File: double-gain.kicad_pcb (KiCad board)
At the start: 2 copper layers, 32 parts, among them J1 Conn_01x01_Female, J2 pin2, J3 Conn_01x01_Female, J4 pin3, J5 pin1, J6 Conn_01x01_Female, J7 Conn_01x01_Female, J8 Conn_01x01_Female, J9 Conn_01x01_Female, U1 NE5534, U2 NE5534

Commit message: Add files via upload
updated files, corrected error
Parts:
- added C9: 22pF, Capacitor_THT:C_Disc_D5.0mm_W2.5mm_P2.50mm, F.Cu at (57.0, 80.0)
- R2: value 30K -> 4K
- R9: value 1K -> 100
- moved U2 2.50 mm to (70.0, 86.0)
- moved U1 2.00 mm to (51.0, 86.0)
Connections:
- U2 pad 2: Net-(R8-Pad2) -> Net-(R2-Pad1)
- U2 pad 3: Net-(R2-Pad1) -> Net-(R8-Pad2)
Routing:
- net Net-(R2-Pad1): track 40.7 -> 51.2 mm, vias 0 -> 1
- net Net-(C9-Pad1): track 0.00 -> 8.23 mm
- net V-: track 113.9 -> 119.7 mm
- net Net-(C9-Pad2): track 0.00 -> 5.74 mm
- net VCC: track 82.5 -> 86.4 mm, vias 0 -> 1
- net Net-(R8-Pad2): track 23.7 -> 20.7 mm
- net Net-(R2-Pad2): track 23.0 -> 25.8 mm
- net Net-(C5-Pad1): track 43.7 -> 45.7 mm
- net Earth: vias 4 -> 5
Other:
- board outline added: 37.5 x 97.5 mm
- board text added: "R2 Gain values in dB: 2K=26,3K=29,4K=32,5K=34,6K=35, 7K=37"
- board text removed: "R2 Gain values in dB:20K=26,30K=29,40K=32,50K=34,60K=35"

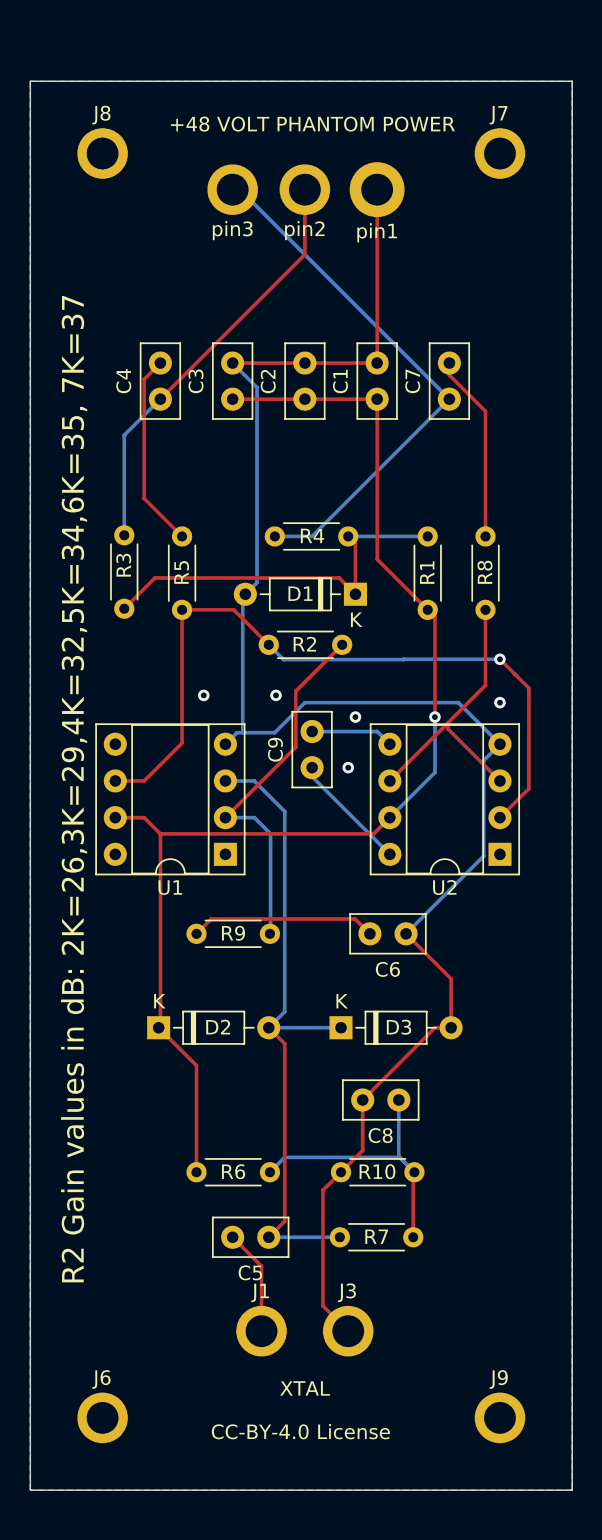
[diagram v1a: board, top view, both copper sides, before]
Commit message: Add files via upload
Converted to balanced input and output.
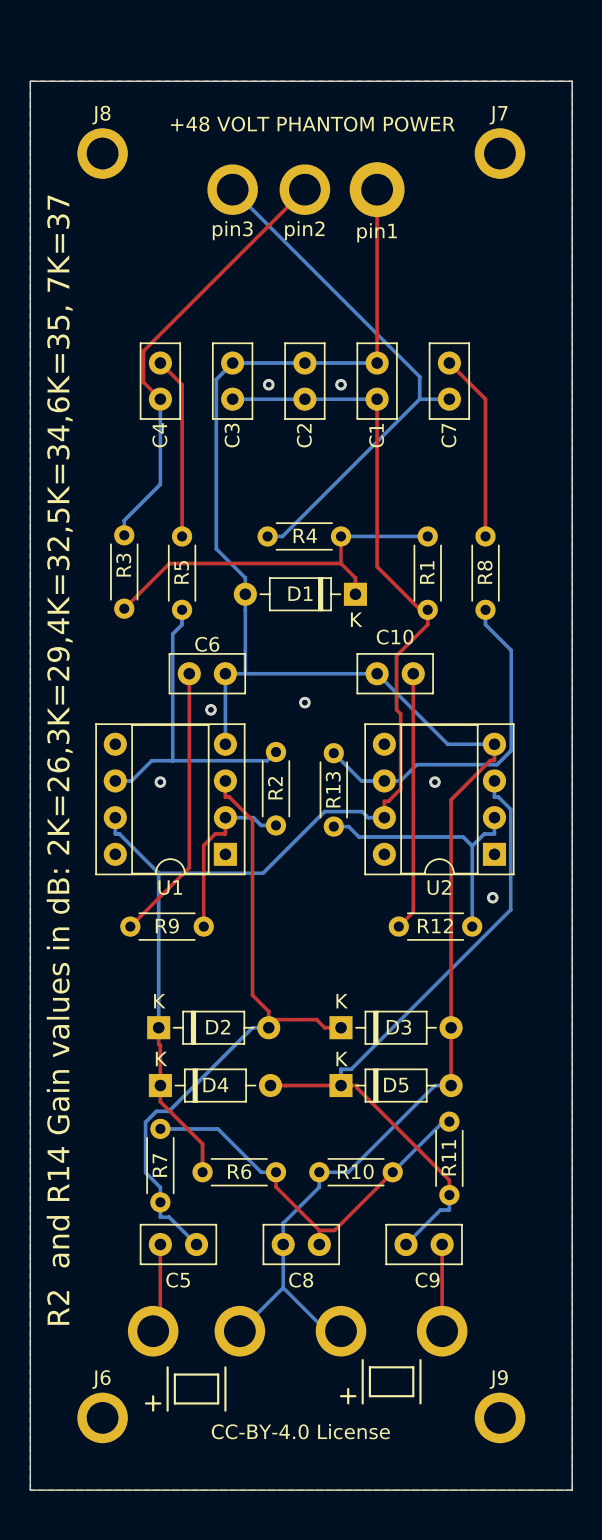
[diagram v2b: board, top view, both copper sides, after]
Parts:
- added C10: 47uF, Capacitor_THT:C_Disc_D5.0mm_W2.5mm_P2.50mm, F.Cu at (61.5, 73.5)
- added D4: 1N4148, Diode_THT:D_DO-35_SOD27_P7.62mm_Horizontal, F.Cu at (46.5, 102.0)
- added D5: 1N4148, Diode_THT:D_DO-35_SOD27_P7.62mm_Horizontal, F.Cu at (59.0, 102.0)
- added J10: Conn_01x01_Female, MountingHole:MountingHole_2.2mm_M2_ISO7380_Pad, F.Cu at (66.0, 119.0)
- added J11: Conn_01x01_Female, MountingHole:MountingHole_2.2mm_M2_ISO7380_Pad, F.Cu at (59.0, 119.0)
- added R11: 1M, Resistor_THT:R_Axial_DIN0204_L3.6mm_D1.6mm_P5.08mm_Horizontal, F.Cu at (66.5, 104.5)
- added R12: 100, Resistor_THT:R_Axial_DIN0204_L3.6mm_D1.6mm_P5.08mm_Horizontal, F.Cu at (63.0, 91.0)
- added R13: 4K, Resistor_THT:R_Axial_DIN0204_L3.6mm_D1.6mm_P5.08mm_Horizontal, F.Cu at (58.5, 79.0)
- C9: value 22pF -> 10uF
- D1: value 1N936B ( 9V ) -> 1N4746A (18V)
- moved C9 33.6 mm to (63.5, 113.0), turned to 0 degrees
- moved C6 21.9 mm to (51.0, 73.5)
- moved R7 19.0 mm to (46.5, 105.0), turned to 270 degrees
- moved C8 11.4 mm to (57.5, 113.0)
- moved J1 7.50 mm to (46.0, 119.0)
- moved J3 7.50 mm to (52.0, 119.0)
- moved R2 7.44 mm to (54.5, 78.9), turned to 270 degrees
- moved C5 5.02 mm to (49.0, 113.0)
- moved R9 4.61 mm to (44.4, 91.0)
- moved R10 1.50 mm to (62.6, 108.0)
- moved R4 0.50 mm to (59.0, 64.0)
- moved R6 0.42 mm to (49.4, 108.0)
- moved U2 0.38 mm to (69.6, 86.0)
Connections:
- C9 pad 1: Net-(C9-Pad1) -> ind
- R8 pad 2: Net-(R8-Pad2) -> Net-(R13-Pad1)
- U2 pad 2: Net-(R2-Pad1) -> Net-(R12-Pad2)
- U2 pad 3: Net-(R8-Pad2) -> ind
- U2 pad 5: Net-(C9-Pad2) -> Net-(U2-Pad5)
- U2 pad 6: Net-(R8-Pad2) -> Net-(R13-Pad1)
- U2 pad 8: Net-(C9-Pad1) -> Net-(U2-Pad8)
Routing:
- net ind: track 0.00 -> 48.2 mm
- net Net-(R2-Pad1): track 51.2 -> 22.7 mm, vias 1 -> 0
- net Net-(R13-Pad1): track 0.00 -> 24.4 mm
- net Net-(R8-Pad2): track 20.7 -> 0.00 mm
- net Net-(R12-Pad2): track 0.00 -> 18.7 mm
- net Net-(C10-Pad2): track 0.00 -> 17.9 mm
- net Net-(R2-Pad2): track 25.8 -> 12.3 mm
- net Net-(C9-Pad1): track 8.23 -> 0.00 mm
- net Net-(C8-Pad1): track 20.8 -> 27.6 mm
- net Net-(C6-Pad2): track 12.8 -> 19.2 mm
- net V-: track 119.7 -> 125.5 mm
- net Net-(C5-Pad2): track 7.33 -> 6.21 mm
- net Net-(C4-Pad1): track 29.1 -> 30.1 mm
- net VCC: track 86.4 -> 87.3 mm, vias 1 -> 0
- net Net-(C4-Pad2): track 13.6 -> 12.6 mm
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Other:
- board text added: "R2 and R14 Gain values in dB: 2K=26,3K=29,4K=32,5K=34,6K=35, 7K=37"
- board text removed: "R2 Gain values in dB: 2K=26,3K=29,4K=32,5K=34,6K=35, 7K=37"
- board text removed: "XTAL"

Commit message: Add files via upload
corrected fault, R14 is R13
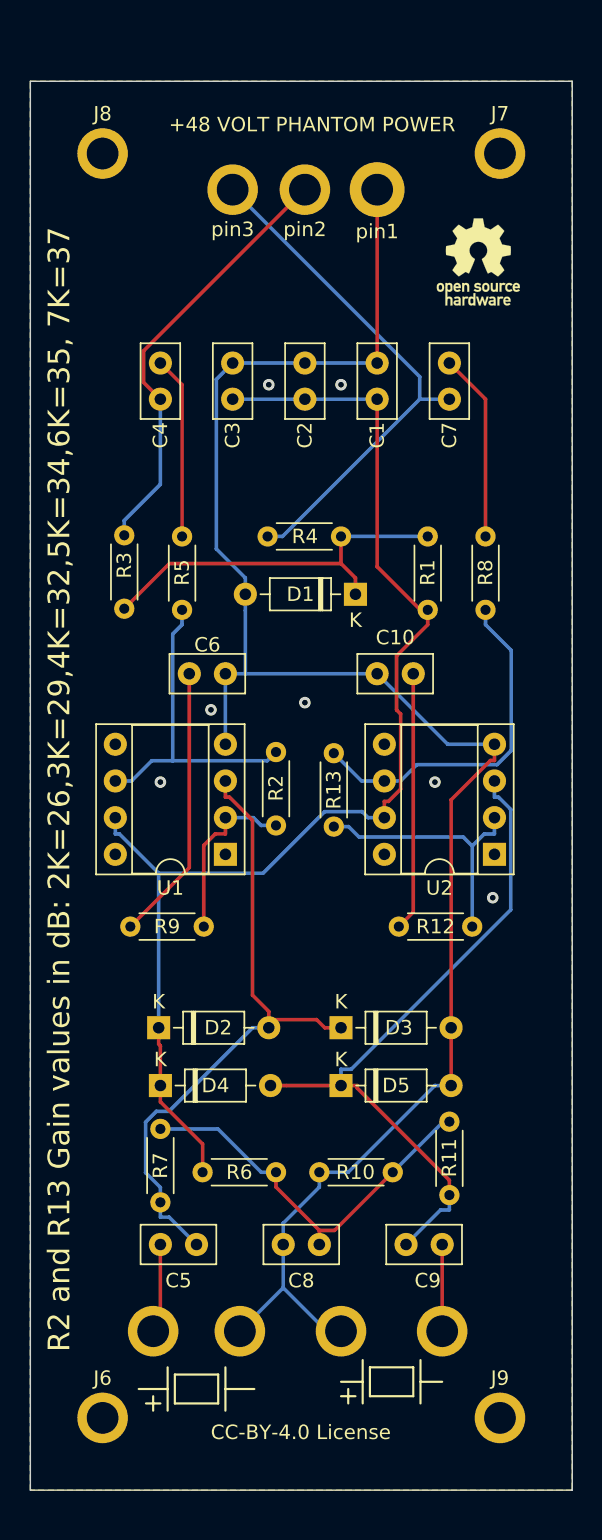
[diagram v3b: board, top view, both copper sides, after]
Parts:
- added REF**: OSHW-Logo_5.7x6mm_SilkScreen, Symbol:OSHW-Logo_5.7x6mm_SilkScreen, F.Cu at (68.5, 45.0)
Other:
- board text added: "R2 and R13 Gain values in dB: 2K=26,3K=29,4K=32,5K=34,6K=35, 7K=37"
- board text removed: "R2 and R14 Gain values in dB: 2K=26,3K=29,4K=32,5K=34,6K=35, 7K=37"

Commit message: Add files via upload
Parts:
- removed REF**: OSHW-Logo_5.7x6mm_SilkScreen, Symbol:OSHW-Logo_5.7x6mm_SilkScreen
- J2: value pin2 -> Conn_01x01_Female
- J4: value pin3 -> Conn_01x01_Female
- J5: value pin1 -> Conn_01x01_Female; footprint MountingHole:MountingHole_2.2mm_M2_DIN965_Pad -> MountingHole:MountingHole_2.2mm_M2_ISO7380_Pad
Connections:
- net Net-(C4-Pad1) renamed /2
- net Net-(C7-Pad1) renamed /3
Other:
- board text added: "pin1"
- board text added: "pin2"
- board text added: "pin3"

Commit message: Add files via upload
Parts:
- added REF**: OSHW-Logo2_14.6x12mm_SilkScreen, Symbol:OSHW-Logo2_14.6x12mm_SilkScreen, F.Cu at (67.5, 45.0)

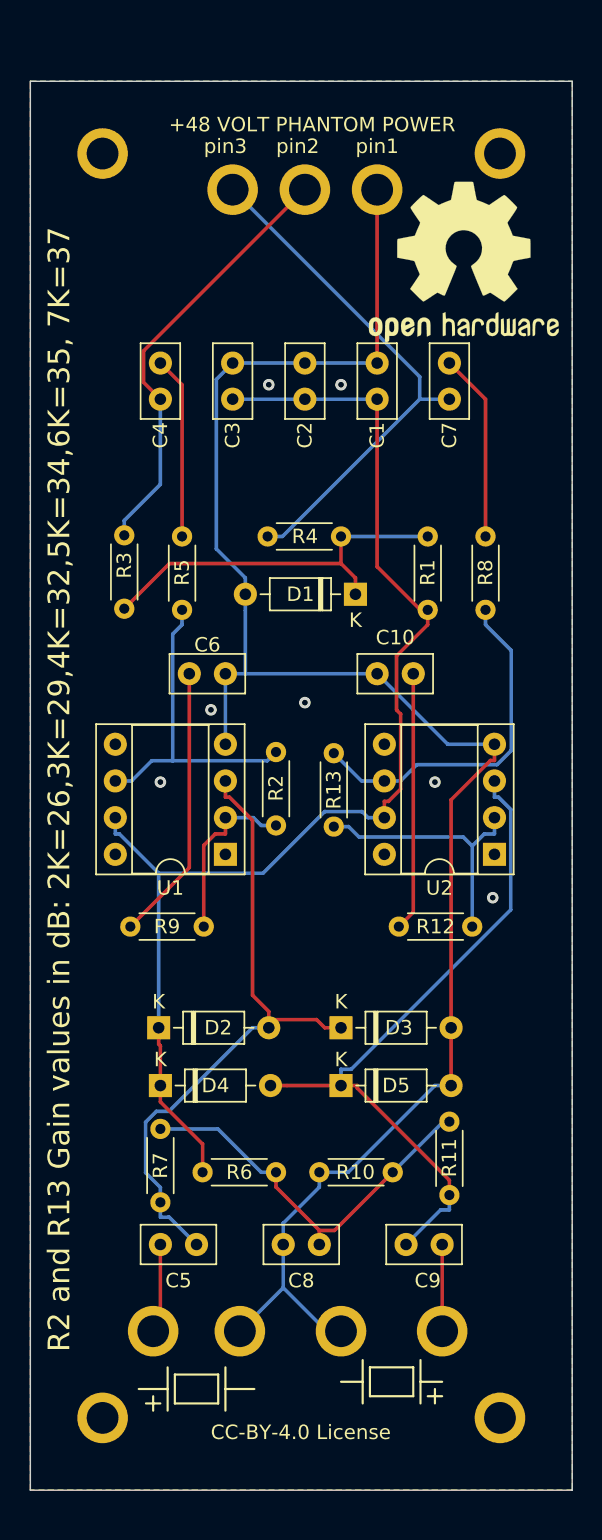
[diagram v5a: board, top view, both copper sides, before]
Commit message: Add files via upload
fixed a error.
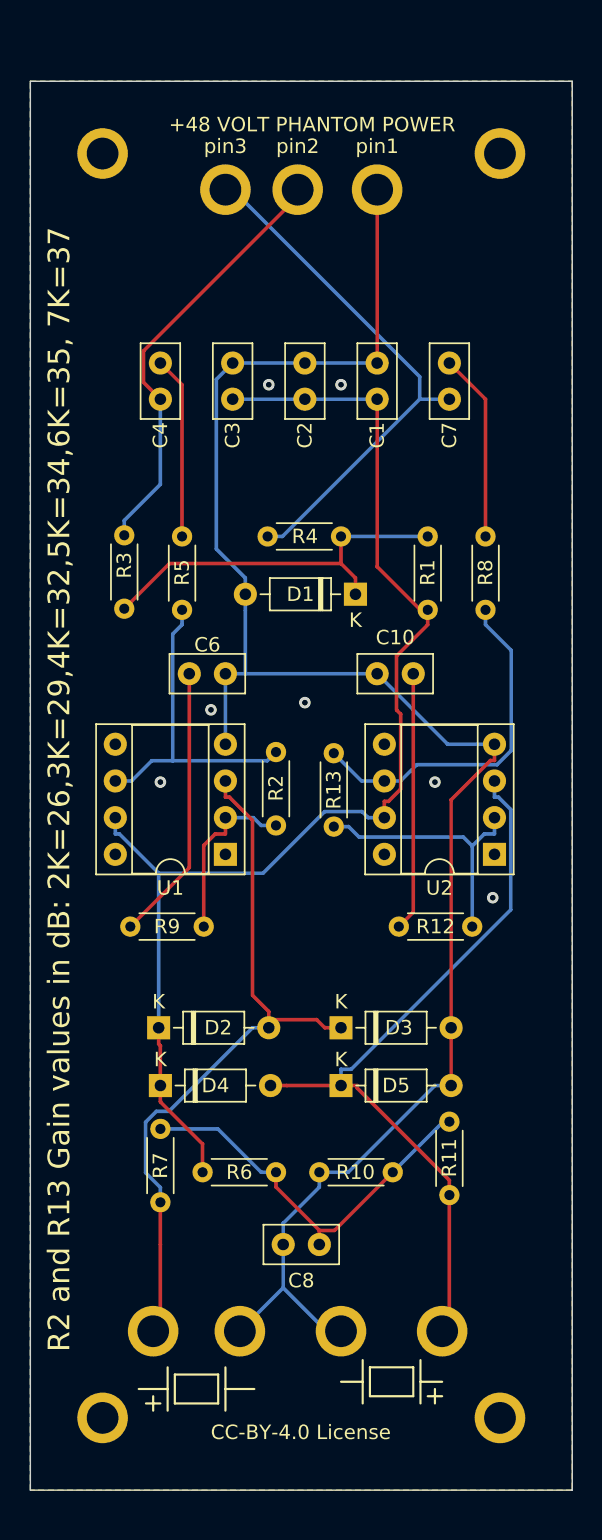
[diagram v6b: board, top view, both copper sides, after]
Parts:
- removed C5, C9: 10uF, Capacitor_THT:C_Disc_D5.0mm_W2.5mm_P2.50mm
- removed REF**: OSHW-Logo2_14.6x12mm_SilkScreen, Symbol:OSHW-Logo2_14.6x12mm_SilkScreen
- moved J2 0.50 mm to (56.0, 40.0)
- moved J4 0.50 mm to (51.0, 40.0)
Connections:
- D2 pad 2: Net-(C5-Pad1) -> Net-(D2-Pad2)
- D3 pad 1: Net-(C5-Pad1) -> Net-(D2-Pad2)
- J1 pad 1: Net-(C5-Pad2) -> Net-(D2-Pad2)
- J10 pad 1: Net-(C9-Pad2) -> ind
- R7 pad 2: Net-(C5-Pad1) -> Net-(D2-Pad2)
- U1 pad 3: Net-(C5-Pad1) -> Net-(D2-Pad2)
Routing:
- net Net-(D2-Pad2): track 0.00 -> 50.1 mm
- net Net-(C5-Pad1): track 45.2 -> 0.00 mm
- net Net-(C5-Pad2): track 6.21 -> 0.00 mm
- net Net-(C9-Pad2): track 6.00 -> 0.00 mm
- net ind: track 48.2 -> 52.8 mm

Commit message: Add files via upload
corrected polarity of the elements.
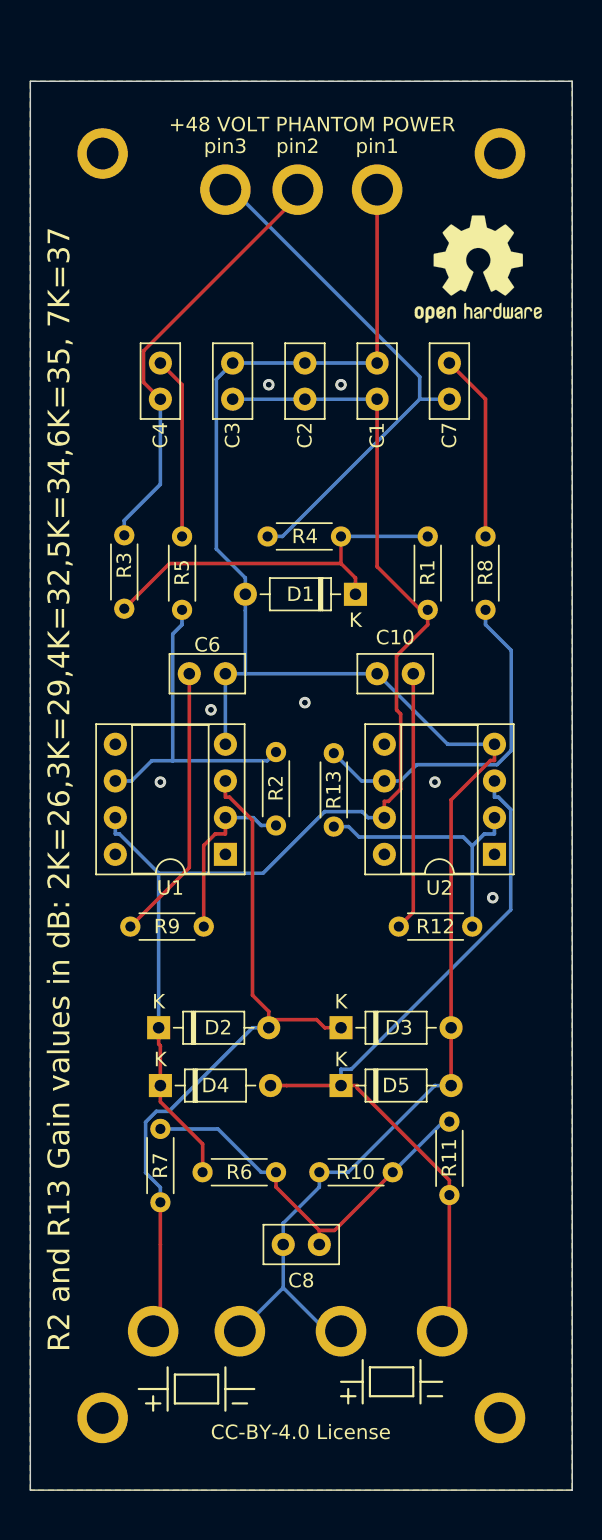
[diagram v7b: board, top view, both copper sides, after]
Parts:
- added REF**: OSHW-Logo2_9.8x8mm_SilkScreen, Symbol:OSHW-Logo2_9.8x8mm_SilkScreen, F.Cu at (68.5, 45.5)

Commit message: Add files via upload
updated files, made traces wider.
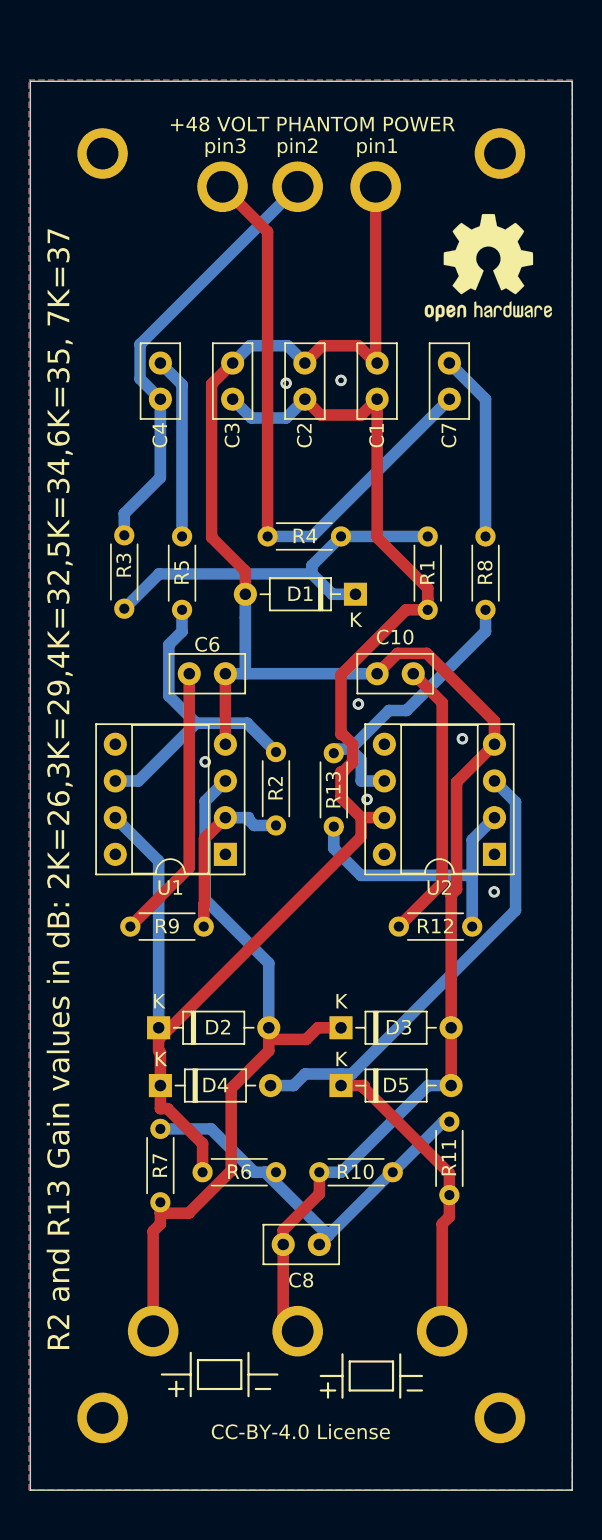
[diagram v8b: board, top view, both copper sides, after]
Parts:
- removed J5: Conn_01x01_Female, MountingHole:MountingHole_2.2mm_M2_ISO7380_Pad
- moved J3 79.2 mm to (50.8, 39.8)
- moved J4 10.4 mm to (61.4, 39.8)
- moved J11 3.00 mm to (56.0, 119.0)
- moved REF** 0.71 mm to (69.2, 45.4)
- moved J2 0.20 mm to (56.0, 39.8)
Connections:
- J3 pad 1: V- -> /3
- J4 pad 1: /3 -> V-
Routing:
- net VCC: track 87.3 -> 97.2 mm
- net /3: track 36.4 -> 42.0 mm
- net Net-(R13-Pad1): track 24.4 -> 19.6 mm
- net Earth: track 0.00 -> 3.04 mm
- net V-: track 125.5 -> 123.8 mm
- net Net-(C10-Pad2): track 17.9 -> 19.6 mm
- net Net-(R12-Pad2): track 18.7 -> 20.0 mm
- net Net-(D2-Pad2): track 50.1 -> 51.0 mm
- net ind: track 52.8 -> 53.6 mm
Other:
- net class Default: trace_width 0.25 -> 0.8
